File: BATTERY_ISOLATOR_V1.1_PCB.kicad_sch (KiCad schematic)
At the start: 42 parts, among them J23 CAN 1, J3 PROG, Q1 AO3400A, Q2 AO3400A, Q3 DMTH4008LPS-13, Q4 DMTH4008LPS-13, Q5 DMTH4008LPS-13, Q6 DMTH4008LPS-13, U1 STM32F042F6Px, U2 ACS724xLCTR-30AB, U3 UA78M33QDCYRQ1, U4 UCC27517DBVR, U5 MCP2551-I-SN, Y2 HSE

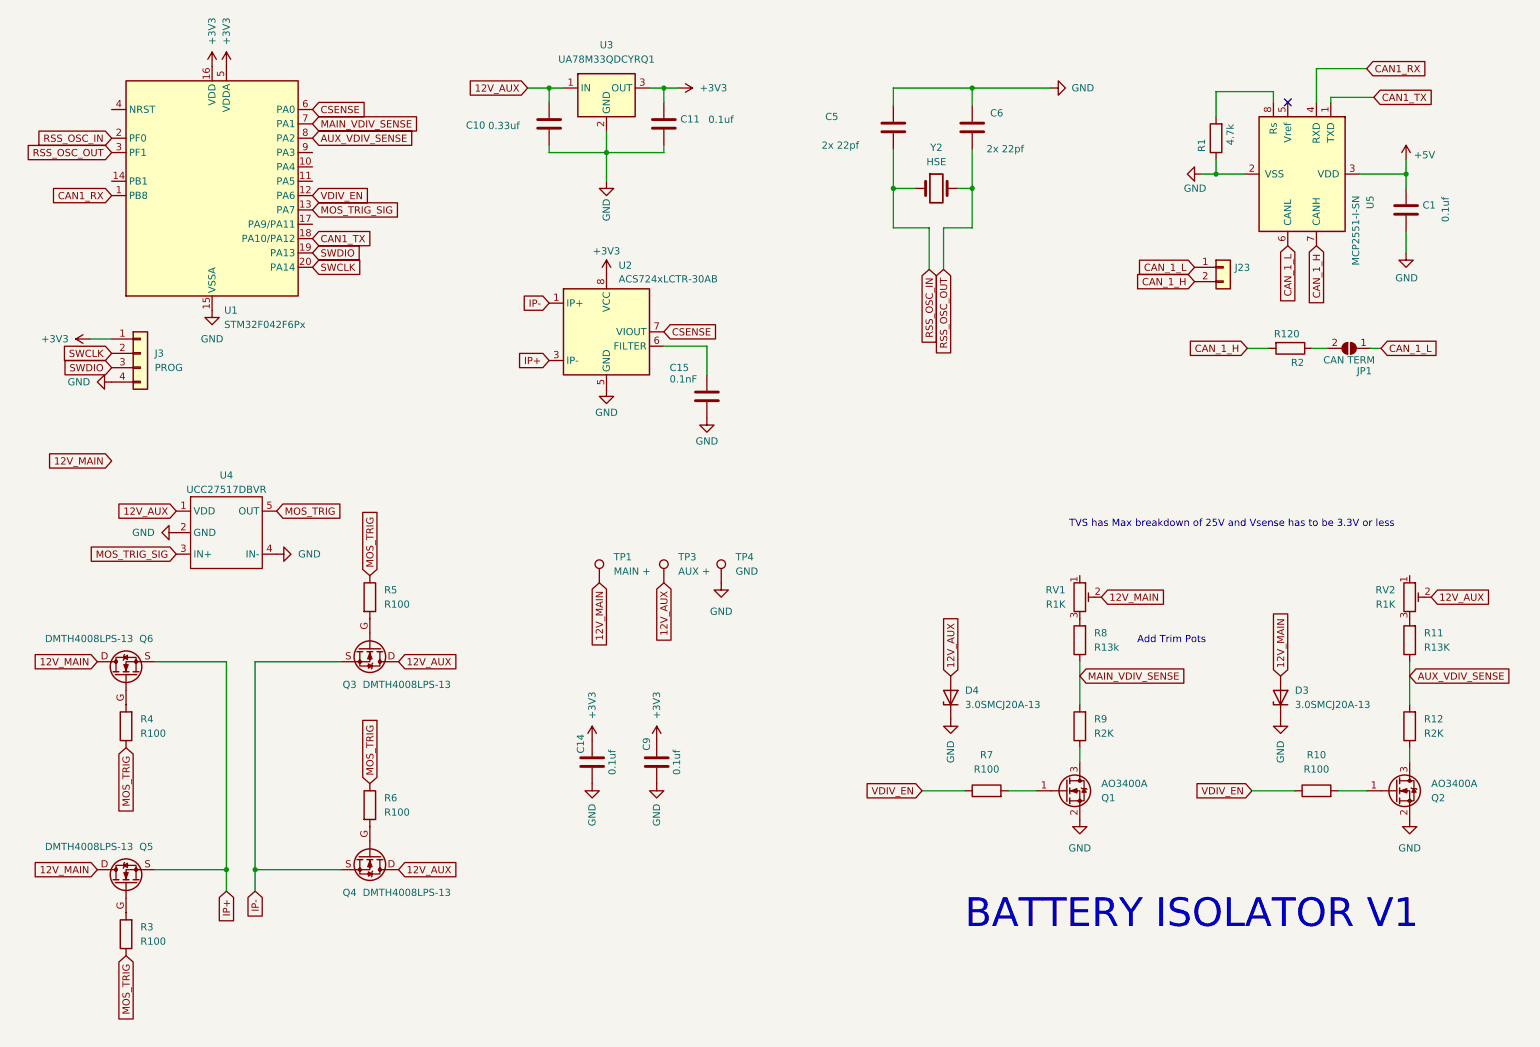
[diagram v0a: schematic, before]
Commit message: Added bicolor LED and Switch 3V3 source to 12V Main
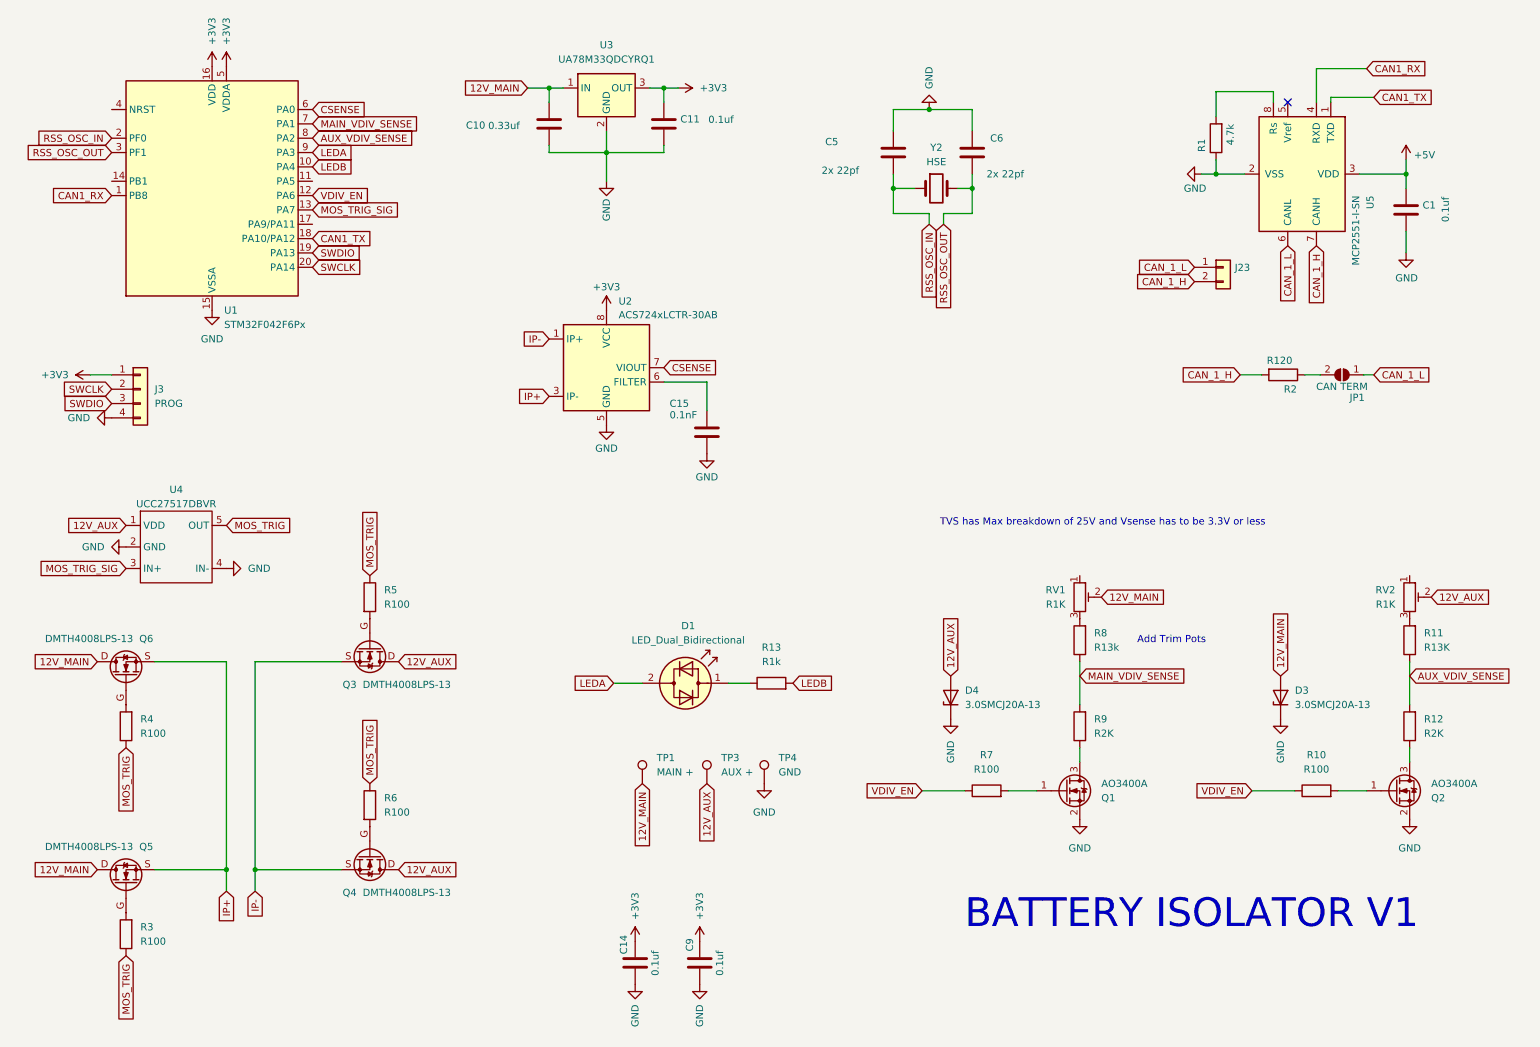
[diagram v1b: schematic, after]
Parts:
- added D1: LED_Dual_Bidirectional, LED_THT:LED_D5.0mm, symbol Device:LED_Dual_Bidirectional
- added R13: R1k, Resistor_SMD:R_0603_1608Metric, symbol Device:R
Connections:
- net 12V_AUX: no longer C10.1, U3.1 (IN)
- net 12V_MAIN: now also C10.1, U3.1 (IN)
- net LEDB: now reaches U1.10 (PA4)
- net LEDB: now also R13.2
- net LEDA: now reaches U1.9 (PA3)
- net LEDA: now also D1.2 (AK)
- new net: D1.1 (KA), R13.1
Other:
- moved on the sheet: C14, C15, C5, C6, C9, J3, JP1, R2, TP1, TP3, TP4, U2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
